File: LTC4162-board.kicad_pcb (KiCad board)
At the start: 2 copper layers, 59.2 x 25.1 mm, 67 parts, among them J2 Conn_01x02, J3 Conn_02x03_Odd_Even, J4 Conn_01x02, Q1 Q_NMOS_GDS, Q2 Q_NMOS_GDS, U1 LTC4162-L

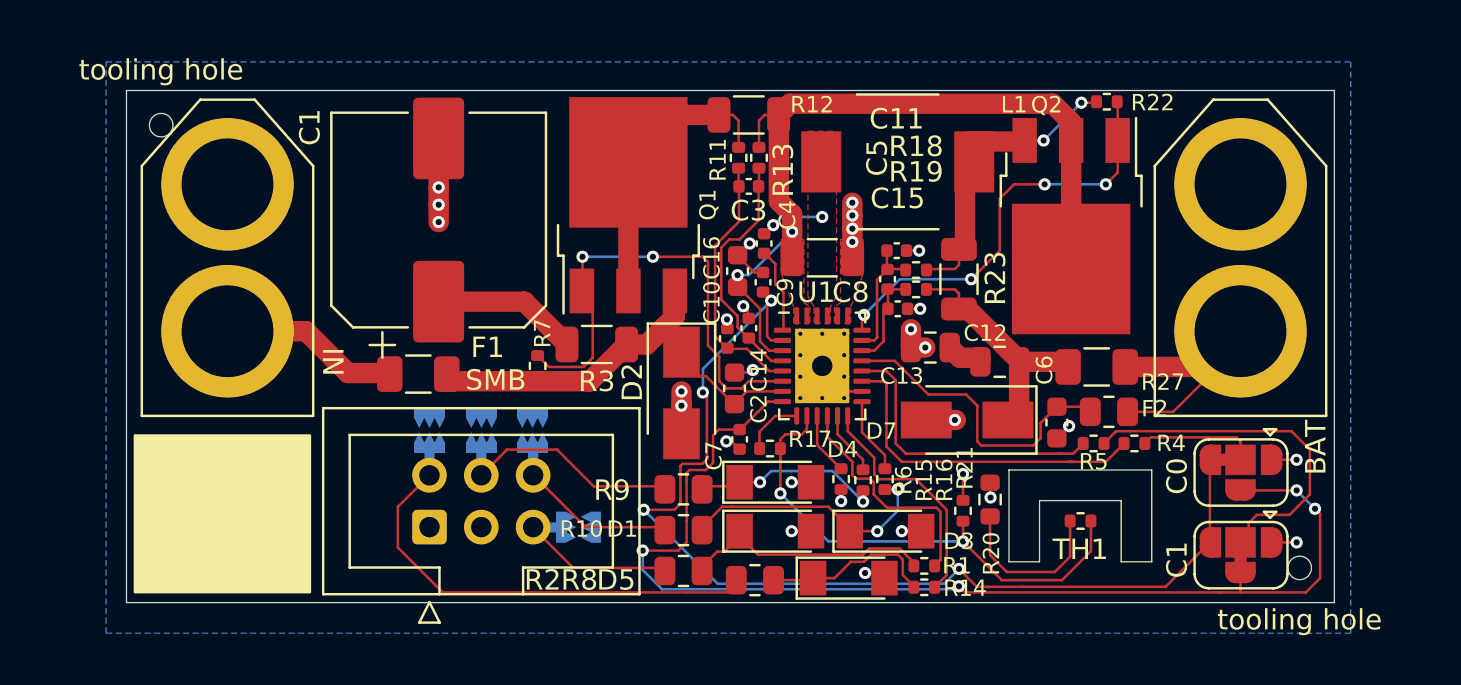
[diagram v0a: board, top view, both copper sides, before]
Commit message: Optimize for basic parts
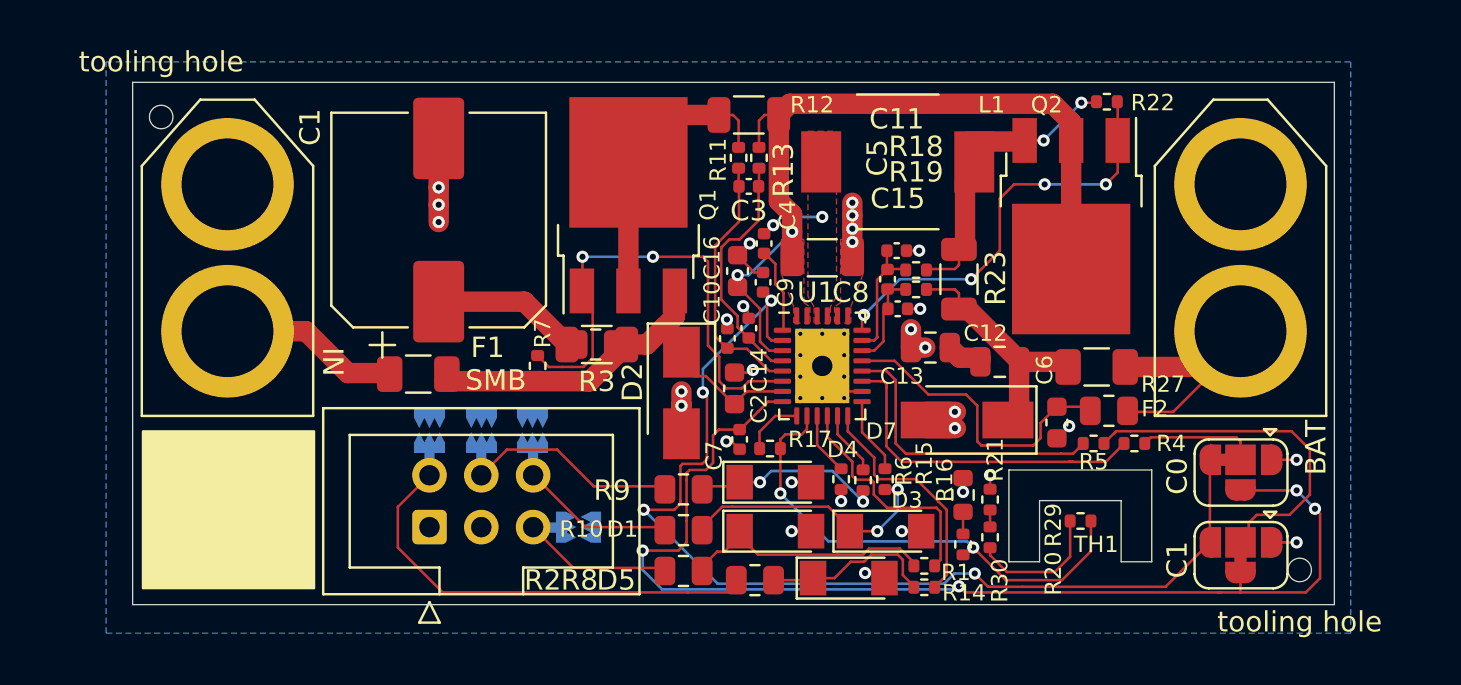
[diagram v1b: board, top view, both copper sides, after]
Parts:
- added R28: 2.2R, Resistor_SMD:R_0805_2012Metric, F.Cu at (130.0, 128.8)
- added R29: 33R, Resistor_SMD:R_0402_1005Metric, F.Cu at (149.3, 136.4)
- added R30: 27kR, Resistor_SMD:R_0402_1005Metric, F.Cu at (148.0, 138.7)
- C10, C11, C14, C15: value 100nF -> 100nF HV 0402
- C16, C2, C6: value 100nF -> 100nF HV
- R20: value 549R -> 510R; footprint Resistor_SMD:R_0603_1608Metric -> Resistor_SMD:R_0402_1005Metric
- R21: value 187kR -> 160kR; footprint Resistor_SMD:R_0402_1005Metric -> Resistor_SMD:R_0603_1608Metric
- R3: value 2.5 R -> DNP
- moved R20 1.85 mm to (149.3, 138.3)
- moved R21 0.78 mm to (148.0, 136.2)
- moved R24 0.54 mm to (112.0, 135.1)
- moved R25 0.54 mm to (112.0, 137.5)
- moved R26 0.54 mm to (112.0, 139.9)
- moved H2 0.40 mm to (108.7, 117.7)
- moved H1 0.10 mm to (164.5, 139.9)
- moved R27 0.05 mm to (155.2, 132.1)
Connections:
- R20 pad 1: GND -> Net-(R20-Pad1)
- R21 pad 1: Net-(R17-Pad1) -> Net-(R21-Pad1)
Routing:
- net Net-(R20-Pad2): track 8.23 -> 6.70 mm
- net Net-(R21-Pad1): track 0.00 -> 1.06 mm
- net Net-(R20-Pad1): track 0.00 -> 0.84 mm
- net GND: track 30.1 -> 30.9 mm, vias 29 -> 30
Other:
- board size 59.2 x 25.1 mm -> 58.9 x 25.6 mm

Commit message: Improve bypassing
* Replace input wet electrolytic by solid polymer cap
* Bypass charge output with wet electrolytic
* Bypass both output and batsense+ with 10uF MLCC
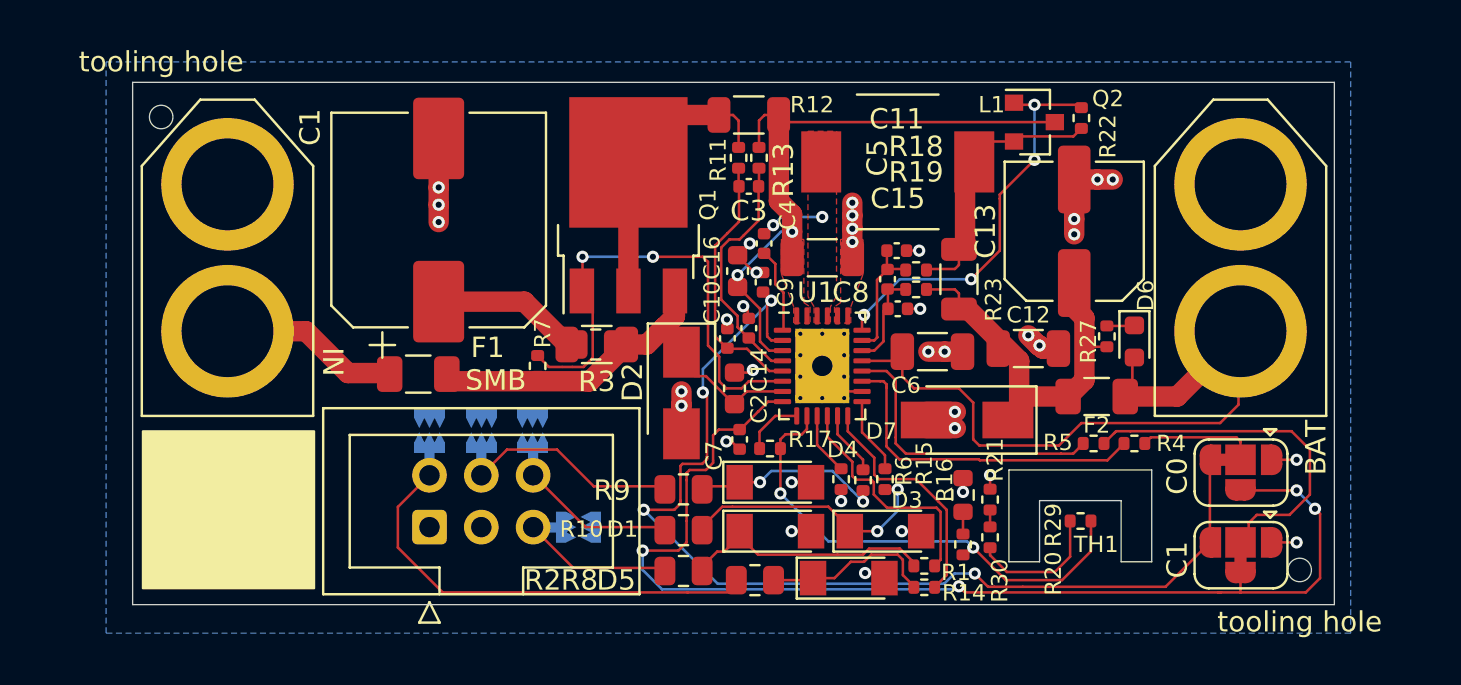
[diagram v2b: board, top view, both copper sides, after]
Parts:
- added D6: LED GRN, LED_SMD:LED_0603_1608Metric, F.Cu at (156.4, 128.7)
- C1: value 220 uF -> 100uF
- C10, C11, C14, C15: value 100nF HV 0402 -> 33nF
- C12: value 22 uF -> 10uF HV; footprint Capacitor_SMD:C_0805_2012Metric -> Capacitor_SMD:C_1206_3216Metric
- C13: value 22 uF -> CP; footprint Capacitor_SMD:C_0805_2012Metric -> Capacitor_SMD:C_Elec_6.3x7.7
- C6: value 100nF HV -> 10uF HV; footprint Capacitor_SMD:C_0603_1608Metric -> Capacitor_SMD:C_1206_3216Metric
- Q2: value Q_NMOS_GDS -> 2N7002K; footprint Package_TO_SOT_SMD:TO-252-3_TabPin2 -> Package_TO_SOT_SMD:SOT-23
- R27: value 200R -> 10kR; footprint Resistor_SMD:R_0805_2012Metric -> Resistor_SMD:R_0402_1005Metric
- R6: value 63.4kR -> 68kR
- moved C13 9.07 mm to (153.4, 123.3), turned to 90 degrees
- moved C6 7.02 mm to (146.5, 129.2), turned to 0 degrees
- moved Q2 5.41 mm to (151.5, 118.0), turned to 0 degrees
- moved R27 3.65 mm to (155.1, 128.4), turned to 270 degrees
- moved C12 1.54 mm to (151.2, 129.1), turned to 0 degrees
- moved R22 1.48 mm to (153.8, 117.8), turned to 90 degrees
- moved F2 1.45 mm to (154.6, 131.4)
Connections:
- C12 pad 2: Net-(C12-Pad2) -> GND
- C13 pad 1: Net-(C12-Pad2) -> /BSHUNT-
- F2 pad 1: Net-(F2-Pad1) -> /BAT+
- J4 pad 2: Net-(F2-Pad1) -> /BAT+
- Q2 pad 2: CSHUNT- -> /BSHUNT+
- Q2 pad 3: /BSHUNT+ -> CSHUNT-
- R27 pad 1: /BAT+ -> Net-(D6-Pad1)
- R27 pad 2: Net-(F2-Pad1) -> /BSHUNT-
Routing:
- net /BAT+: track 15.2 -> 37.8 mm
- net Net-(F2-Pad1): track 14.0 -> 0.00 mm
- net /BSHUNT-: track 11.9 -> 20.4 mm
- net CSHUNT-: track 40.2 -> 31.9 mm
- net GND: track 30.9 -> 36.4 mm, vias 30 -> 36
- net Net-(C12-Pad2): track 1.91 -> 0.00 mm
- net /BSHUNT+: track 14.5 -> 12.9 mm, vias 2 -> 0
- net Net-(D6-Pad1): track 0.00 -> 1.40 mm
- net Net-(Q2-Pad1): track 20.9 -> 20.0 mm
